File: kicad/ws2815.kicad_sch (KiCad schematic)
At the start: 2 parts

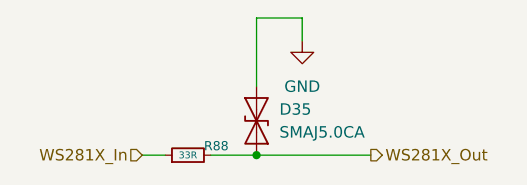
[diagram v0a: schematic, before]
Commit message: Update SCCS-RPI KiCad design and production files
Add GPS RF ESD and matching (ESD103-B1-02EL, 27nH, 10R, 100nF),
swap the 10A fuses to A16-1000, retune copper zone fills, and
regenerate BOM, positions, netlist, gerbers, and schematics PDF.
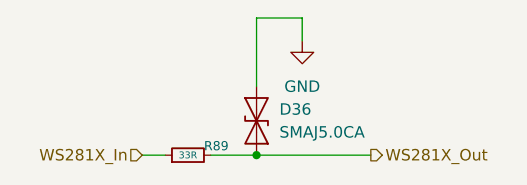
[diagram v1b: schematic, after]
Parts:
- renumbered D35 to D36, R88 to R89
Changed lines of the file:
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@@
 		(in_pos_files yes)
 		(dnp no)
-		(property "Reference" "R88"
+		(property "Reference" "R89"
 			(at 149.098 99.314 90)
 			(show_name no)
@@
 			(project "SCCS-RPI"
 				(path "/ce21946f-7655-4864-b48a-50deff8538eb/ca3e75a4-69fa-4118-99c0-ffa695db17b0"
-					(reference "R88")
+					(reference "R89")
 					(unit 1)
 				)
 				(path "/ce21946f-7655-4864-b48a-50deff8538eb/ecbbfcd6-f58c-4962-8970-f2896585c8c2"
-					(reference "R89")
+					(reference "R90")
 					(unit 1)
 				)
@@
 		(dnp no)
 		(fields_autoplaced yes)
-		(property "Reference" "D35"
+		(property "Reference" "D36"
 			(at 157.48 95.2499 90)
 			(show_name no)
@@
 			(project "SCCS-RPI"
 				(path "/ce21946f-7655-4864-b48a-50deff8538eb/ca3e75a4-69fa-4118-99c0-ffa695db17b0"
-					(reference "D35")
+					(reference "D36")
 					(unit 1)
 				)
 				(path "/ce21946f-7655-4864-b48a-50deff8538eb/ecbbfcd6-f58c-4962-8970-f2896585c8c2"
-					(reference "D36")
+					(reference "D37")
 					(unit 1)
 				)

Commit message: Update SCCS-RPI KiCad design and production files
Split 5V and 3V3 regulation onto dedicated Power sheets with a second
AP64501 buck, extra inductor and passives, update the enclosure
bracket, and regenerate BOM, positions, netlist, gerbers, and
schematics PDF.
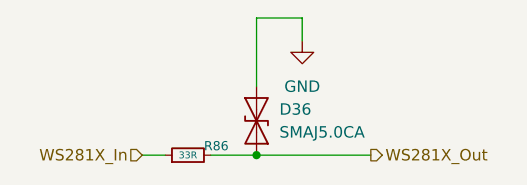
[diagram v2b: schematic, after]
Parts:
- renumbered R89 to R86
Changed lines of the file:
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@@
 		(dnp no)
 		(fields_autoplaced yes)
-		(property "Reference" "#PWR0109"
+		(property "Reference" "#PWR0108"
 			(at 160.02 93.98 0)
 			(hide yes)
@@
 			(project "SCCS-RPI"
 				(path "/ce21946f-7655-4864-b48a-50deff8538eb/ca3e75a4-69fa-4118-99c0-ffa695db17b0"
-					(reference "#PWR0109")
+					(reference "#PWR0108")
 					(unit 1)
 				)
 				(path "/ce21946f-7655-4864-b48a-50deff8538eb/ecbbfcd6-f58c-4962-8970-f2896585c8c2"
-					(reference "#PWR0110")
+					(reference "#PWR0109")
 					(unit 1)
 				)
@@
 		(in_pos_files yes)
 		(dnp no)
-		(property "Reference" "R89"
+		(property "Reference" "R86"
 			(at 149.098 99.314 90)
 			(show_name no)
@@
 			(project "SCCS-RPI"
 				(path "/ce21946f-7655-4864-b48a-50deff8538eb/ca3e75a4-69fa-4118-99c0-ffa695db17b0"
-					(reference "R89")
+					(reference "R86")
 					(unit 1)
 				)
 				(path "/ce21946f-7655-4864-b48a-50deff8538eb/ecbbfcd6-f58c-4962-8970-f2896585c8c2"
-					(reference "R90")
+					(reference "R87")
 					(unit 1)
 				)
